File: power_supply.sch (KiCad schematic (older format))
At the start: 22 parts, among them U1 NCV1117DT, U2 NCV1117ST

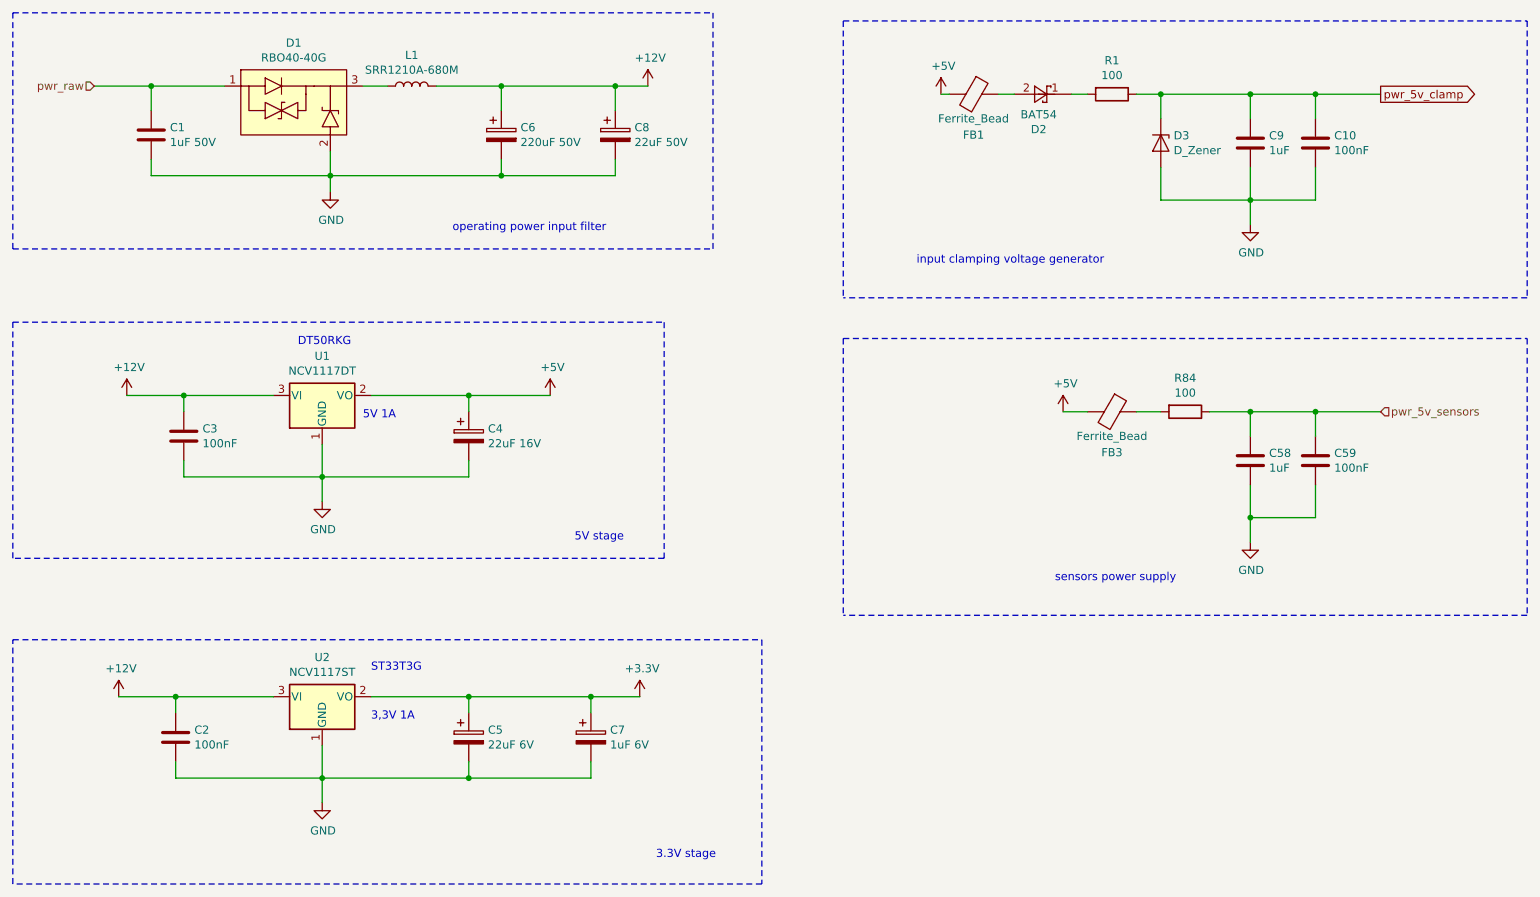
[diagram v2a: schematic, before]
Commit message: added missing component values working on BOM
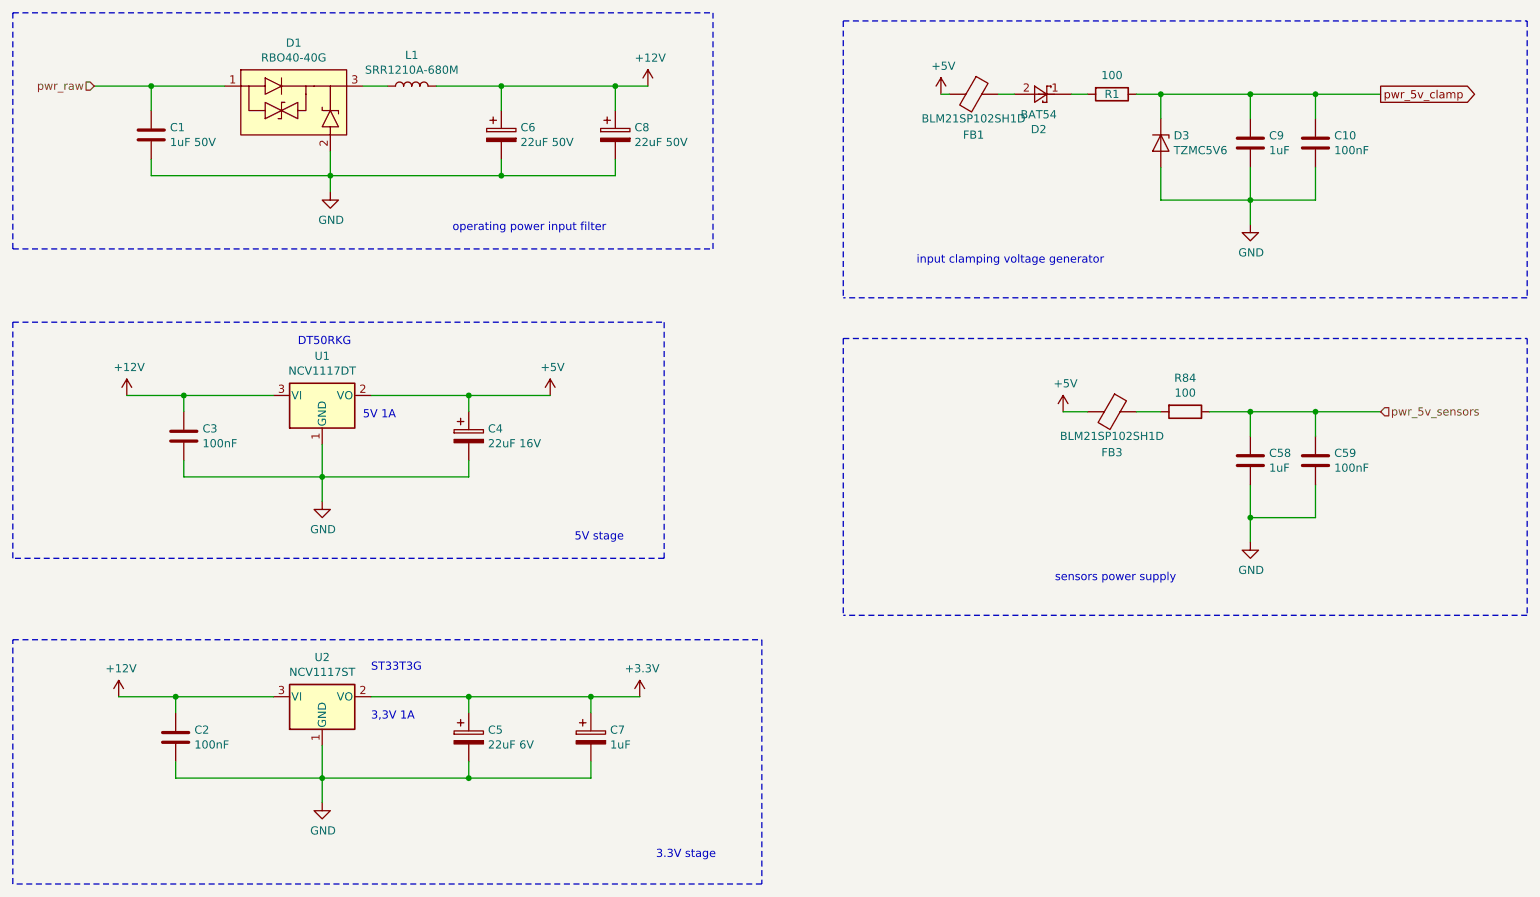
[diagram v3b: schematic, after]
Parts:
- C1: Mouser (none) -> 963-UMK212BJ105KG-T
- C10, C2, C3, C59: Mouser (none) -> 80-C0805C104Z3V
- C4: Mouser (none) -> 667-EEE-FC1C220R
- C5: Mouser (none) -> 667-EEE-HC0J220R
- C58, C9: Mouser (none) -> 80-C0805C105M4R
- C6: value 220uF 50V -> 22uF 50V; Mouser (none) -> 667-EEE-HC1H220XP
- C7: value 1uF 6V -> 1uF; Mouser (none) -> 80-C0805C105M4R
- C8: Mouser (none) -> 667-EEE-HC1H220XP
- D3: value D_Zener -> TZMC5V6
- FB1, FB3: value Ferrite_Bead -> BLM21SP102SH1D
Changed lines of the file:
@@
 F 2 "Capacitor_SMD:C_0805_2012Metric" H 1688 1450 50  0001 C CNN
 F 3 "~" H 1650 1600 50  0001 C CNN
+F 4 "963-UMK212BJ105KG-T" H 1650 1600 50  0001 C CNN "Mouser"
 	1    1650 1600
 	1    0    0    -1
@@
 P 3800 1600
 F 0 "C6" H 3918 1646 50  0000 L CNN
-F 1 "220uF 50V" H 3918 1555 50  0000 L CNN
+F 1 "22uF 50V" H 3918 1555 50  0000 L CNN
 F 2 "Capacitor_SMD:CP_Elec_6.3x7.7" H 3838 1450 50  0001 C CNN
 F 3 "~" H 3800 1600 50  0001 C CNN
+F 4 "667-EEE-HC1H220XP " H 3800 1600 50  0001 C CNN "Mouser"
 	1    3800 1600
 	1    0    0    -1
@@
 F 2 "Capacitor_SMD:C_0805_2012Metric" H 1888 3300 50  0001 C CNN
 F 3 "~" H 1850 3450 50  0001 C CNN
+F 4 "80-C0805C104Z3V " H 1850 3450 50  0001 C CNN "Mouser"
 	1    1850 3450
 	1    0    0    -1
@@
 F 2 "Capacitor_SMD:CP_Elec_5x5.8" H 3638 3300 50  0001 C CNN
 F 3 "~" H 3600 3450 50  0001 C CNN
+F 4 "667-EEE-FC1C220R " H 3600 3450 50  0001 C CNN "Mouser"
 	1    3600 3450
 	1    0    0    -1
@@
 F 2 "Capacitor_SMD:C_0805_2012Metric" H 1838 5150 50  0001 C CNN
 F 3 "~" H 1800 5300 50  0001 C CNN
+F 4 "80-C0805C104Z3V " H 1800 5300 50  0001 C CNN "Mouser"
 	1    1800 5300
 	1    0    0    -1
@@
 F 2 "Capacitor_SMD:CP_Elec_4x5.8" H 3638 5150 50  0001 C CNN
 F 3 "~" H 3600 5300 50  0001 C CNN
+F 4 "667-EEE-HC0J220R " H 3600 5300 50  0001 C CNN "Mouser"
 	1    3600 5300
 	1    0    0    -1
@@
 P 4350 5300
 F 0 "C7" H 4468 5346 50  0000 L CNN
-F 1 "1uF 6V" H 4468 5255 50  0000 L CNN
+F 1 "1uF" H 4468 5255 50  0000 L CNN
 F 2 "Capacitor_SMD:C_0805_2012Metric" H 4388 5150 50  0001 C CNN
 F 3 "~" H 4350 5300 50  0001 C CNN
+F 4 "80-C0805C105M4R " H 4350 5300 50  0001 C CNN "Mouser"
 	1    4350 5300
 	1    0    0    -1
@@
 P 6700 1350
 F 0 "FB1" V 6950 1350 50  0000 C CNN
-F 1 "Ferrite_Bead" V 6850 1350 50  0000 C CNN
+F 1 "BLM21SP102SH1D" V 6850 1350 50  0000 C CNN
 F 2 "Inductor_SMD:L_0805_2012Metric" V 6630 1350 50  0001 C CNN
 F 3 "~" H 6700 1350 50  0001 C CNN
@@
 U 1 1 5BCBA833
 P 7550 1350
-F 0 "R1" V 7343 1350 50  0000 C CNN
+F 0 "R1" V 7550 1350 50  0000 C CNN
 F 1 "100" V 7434 1350 50  0000 C CNN
 F 2 "Resistor_SMD:R_1210_3225Metric" V 7480 1350 50  0001 C CNN
@@
 P 7850 1650
 F 0 "D3" V 7804 1729 50  0000 L CNN
-F 1 "D_Zener" V 7895 1729 50  0000 L CNN
+F 1 "TZMC5V6" V 7895 1729 50  0000 L CNN
 F 2 "Diode_SMD:D_MiniMELF" H 7850 1650 50  0001 C CNN
 F 3 "~" H 7850 1650 50  0001 C CNN
@@
 F 2 "Capacitor_SMD:C_0805_2012Metric" H 8438 1500 50  0001 C CNN
 F 3 "~" H 8400 1650 50  0001 C CNN
+F 4 "80-C0805C105M4R " H 8400 1650 50  0001 C CNN "Mouser"
 	1    8400 1650
 	1    0    0    -1
@@
 F 2 "Capacitor_SMD:C_0805_2012Metric" H 8838 1500 50  0001 C CNN
 F 3 "~" H 8800 1650 50  0001 C CNN
+F 4 "80-C0805C104Z3V " H 8800 1650 50  0001 C CNN "Mouser"
 	1    8800 1650
 	1    0    0    -1
@@
 F 2 "Capacitor_SMD:CP_Elec_6.3x7.7" H 4538 1450 50  0001 C CNN
 F 3 "~" H 4500 1600 50  0001 C CNN
+F 4 "667-EEE-HC1H220XP " H 4500 1600 50  0001 C CNN "Mouser"
 	1    4500 1600
 	1    0    0    -1
@@
 P 7550 3300
 F 0 "FB3" V 7800 3300 50  0000 C CNN
-F 1 "Ferrite_Bead" V 7700 3300 50  0000 C CNN
+F 1 "BLM21SP102SH1D" V 7700 3300 50  0000 C CNN
 F 2 "Inductor_SMD:L_0805_2012Metric" V 7480 3300 50  0001 C CNN
 F 3 "~" H 7550 3300 50  0001 C CNN
@@
 F 2 "Capacitor_SMD:C_0805_2012Metric" H 8438 3450 50  0001 C CNN
 F 3 "~" H 8400 3600 50  0001 C CNN
+F 4 "80-C0805C105M4R " H 8400 3600 50  0001 C CNN "Mouser"
 	1    8400 3600
 	1    0    0    -1
@@
 F 2 "Capacitor_SMD:C_0805_2012Metric" H 8838 3450 50  0001 C CNN
 F 3 "~" H 8800 3600 50  0001 C CNN
+F 4 "80-C0805C104Z3V " H 8800 3600 50  0001 C CNN "Mouser"
 	1    8800 3600
 	1    0    0    -1

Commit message: cleaned BOMs
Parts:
- D1: Mouser (none) -> 511-RBO40-40G
- D2: Mouser (none) -> 755-BAT54HMFHT116
- D3: Mouser (none) -> 78-TZMC5.6
- FB1, FB3: Mouser (none) -> 81-BLM21SP102SH1D
- L1: Mouser (none) -> 652-SRR1210A-680M
- R1, R84: Mouser (none) -> 279-CRGCQ1210F100R
- U1: Mouser (none) -> 863-NCV1117DT50RKG
- U2: Mouser (none) -> 863-NCV1117ST33T3G
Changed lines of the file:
@@
 F 2 "Inductor_SMD:L_0805_2012Metric" V 6630 1350 50  0001 C CNN
 F 3 "~" H 6700 1350 50  0001 C CNN
+F 4 "81-BLM21SP102SH1D" H 6700 1350 50  0001 C CNN "Mouser"
 	1    6700 1350
 	0    1    1    0
@@
 F 2 "Resistor_SMD:R_1210_3225Metric" V 7480 1350 50  0001 C CNN
 F 3 "~" H 7550 1350 50  0001 C CNN
+F 4 "279-CRGCQ1210F100R" H 7550 1350 50  0001 C CNN "Mouser"
 	1    7550 1350
 	0    1    1    0
@@
 F 2 "Diode_SMD:D_MiniMELF" H 7850 1650 50  0001 C CNN
 F 3 "~" H 7850 1650 50  0001 C CNN
+F 4 "78-TZMC5.6" H 7850 1650 50  0001 C CNN "Mouser"
 	1    7850 1650
 	0    1    1    0
@@
 F 2 "boctok_footprints:NCV1117DT" H 2700 3200 50  0001 C CNN
 F 3 "" H 2700 3200 50  0001 C CNN
+F 4 "863-NCV1117DT50RKG" H 2700 3200 50  0001 C CNN "Mouser"
 	1    2700 3200
 	1    0    0    -1
@@
 F 2 "boctok_footprints:NCV1117ST" H 2700 5050 50  0001 C CNN
 F 3 "" H 2700 5050 50  0001 C CNN
+F 4 "863-NCV1117ST33T3G" H 2700 5050 50  0001 C CNN "Mouser"
 	1    2700 5050
 	1    0    0    -1
@@
 F 2 "boctok_footprints:RBO40-40G" H 2600 1650 50  0001 C CNN
 F 3 "~" H 2450 1300 50  0001 C CNN
+F 4 "511-RBO40-40G" H 2600 1300 50  0001 C CNN "Mouser"
 	1    2600 1300
 	1    0    0    -1
@@
 F 2 "boctok_footprints:SRR1210A" V 3100 1200 50  0001 C CNN
 F 3 "~" H 3250 1300 50  0001 C CNN
+F 4 "652-SRR1210A-680M" H 3250 1300 50  0001 C CNN "Mouser"
 	1    3250 1300
 	0    -1   -1   0
@@
 F 2 "Diode_SMD:D_SOT-23_ANK" H 7100 1175 50  0001 C CNN
 F 3 "http://www.vishay.com/docs/88503/1n4001.pdf" H 7100 1350 50  0001 C CNN
+F 4 "755-BAT54HMFHT116" H 7100 1350 50  0001 C CNN "Mouser"
 	1    7100 1350
 	1    0    0    -1
@@
 F 2 "Inductor_SMD:L_0805_2012Metric" V 7480 3300 50  0001 C CNN
 F 3 "~" H 7550 3300 50  0001 C CNN
+F 4 "81-BLM21SP102SH1D" H 7550 3300 50  0001 C CNN "Mouser"
 	1    7550 3300
 	0    1    1    0
@@
 F 2 "Resistor_SMD:R_1210_3225Metric" V 7930 3300 50  0001 C CNN
 F 3 "~" H 8000 3300 50  0001 C CNN
+F 4 "279-CRGCQ1210F100R" H 8000 3300 50  0001 C CNN "Mouser"
 	1    8000 3300
 	0    1    1    0
